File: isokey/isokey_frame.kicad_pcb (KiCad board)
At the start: 2 copper layers, 158.4 x 138.3 mm, 394 parts, among them J1 PJ-320A-4P, J2 PJ-320A-4P, Q2 BSS138, Q3 BSS138, SW1 Cherry, SW10 Cherry, SW11 Cherry, SW12 Cherry, SW13 Cherry, SW14 Cherry, SW15 Cherry, SW16 Cherry, SW17 Cherry, SW18 Cherry, SW19 Cherry, SW2 Cherry, SW20 Cherry, SW21 Cherry, SW22 Cherry, SW23 Cherry, SW24 Cherry, SW25 Cherry, SW26 Cherry, SW27 Cherry, SW28 Cherry, SW29 Cherry, SW3 Cherry, SW30 Cherry, SW31 Cherry, SW32 Cherry, SW33 Cherry, SW34 Cherry, SW35 Cherry, SW36 Cherry, SW37 Cherry, SW38 Cherry, SW39 Cherry, SW4 Cherry, SW40 Cherry, SW41 Cherry, SW42 Cherry, SW43 Cherry, SW44 Cherry, SW45 Cherry, SW46 Cherry, SW47 Cherry, SW48 Cherry, SW5 Cherry, SW6 Cherry, SW7 Cherry, SW8 Cherry, SW9 Cherry, U1 BlackPill_STLINK, U3 TLV73318PDBV, U6 JOYSTICKPTH, U7 JOYSTICKPTH, U9 TLV73318PDBV

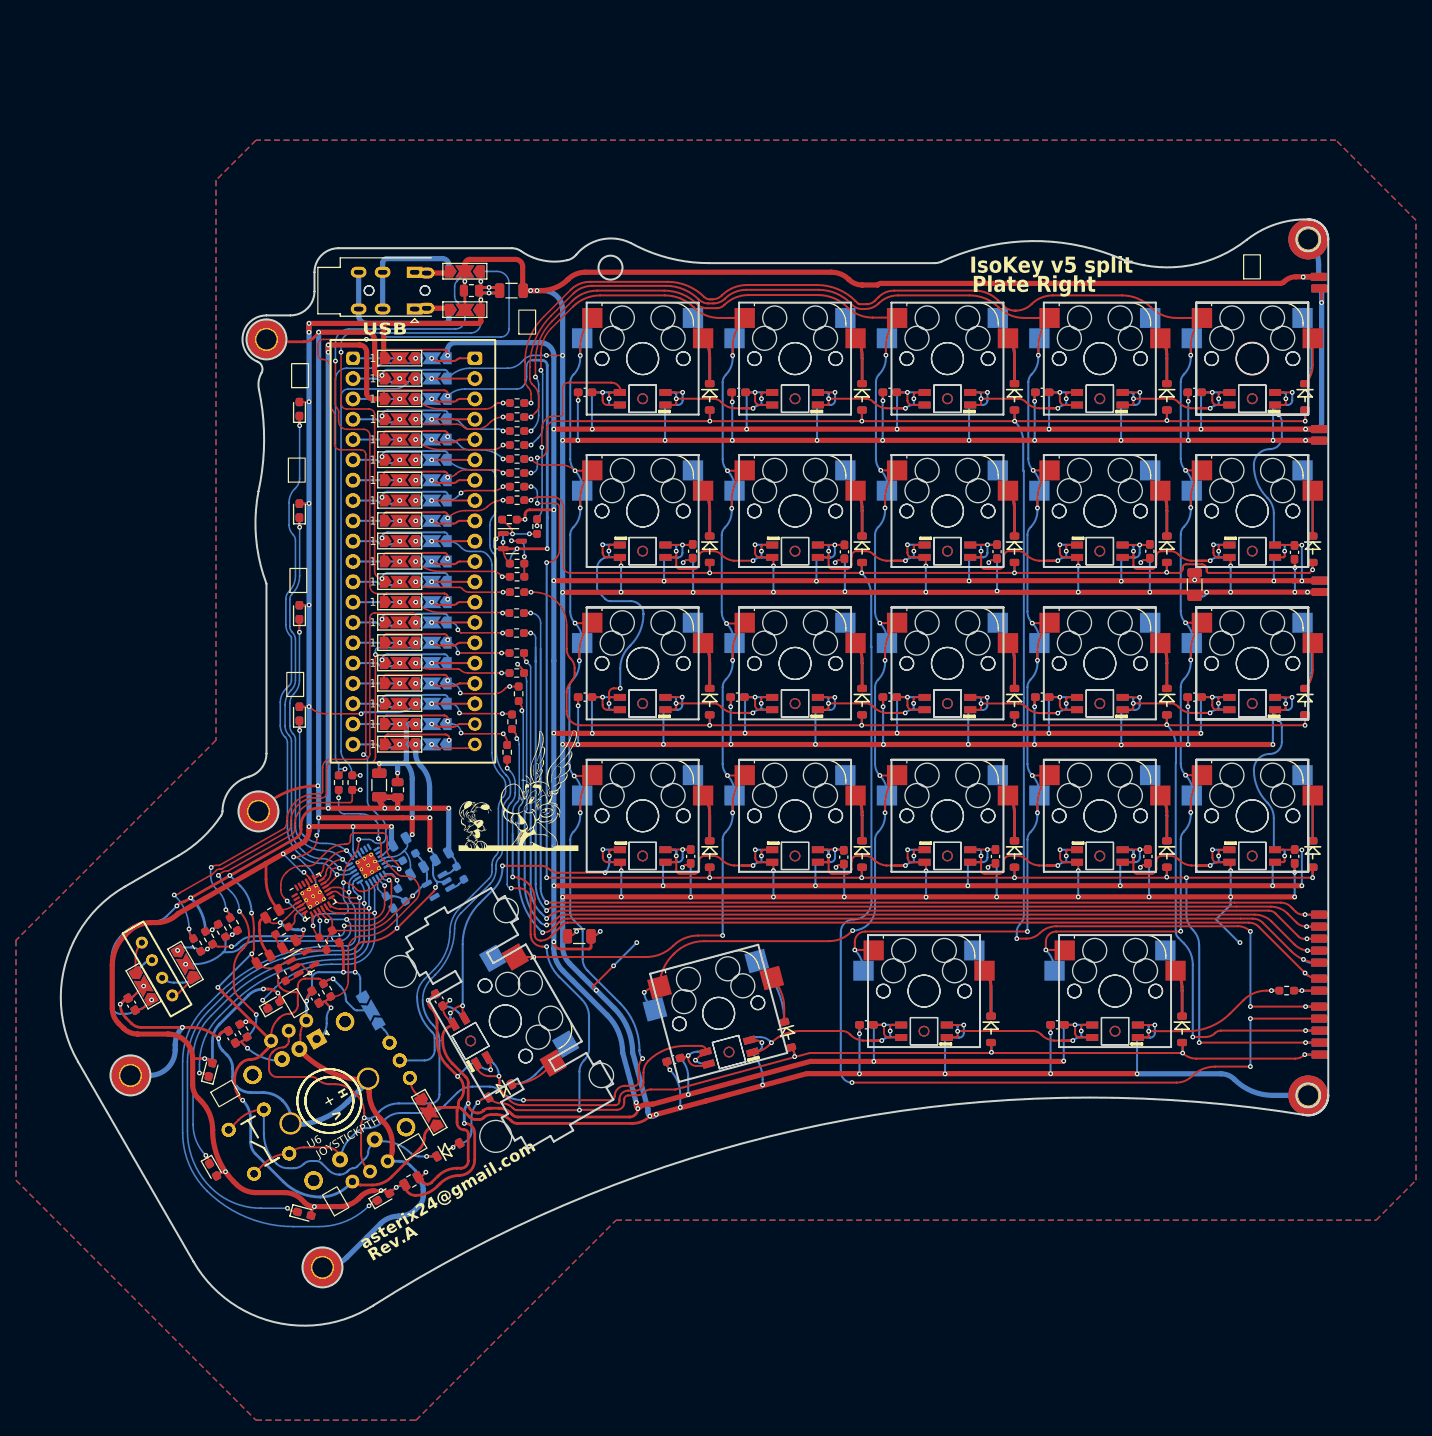
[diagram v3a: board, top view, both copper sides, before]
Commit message: add frame pcb
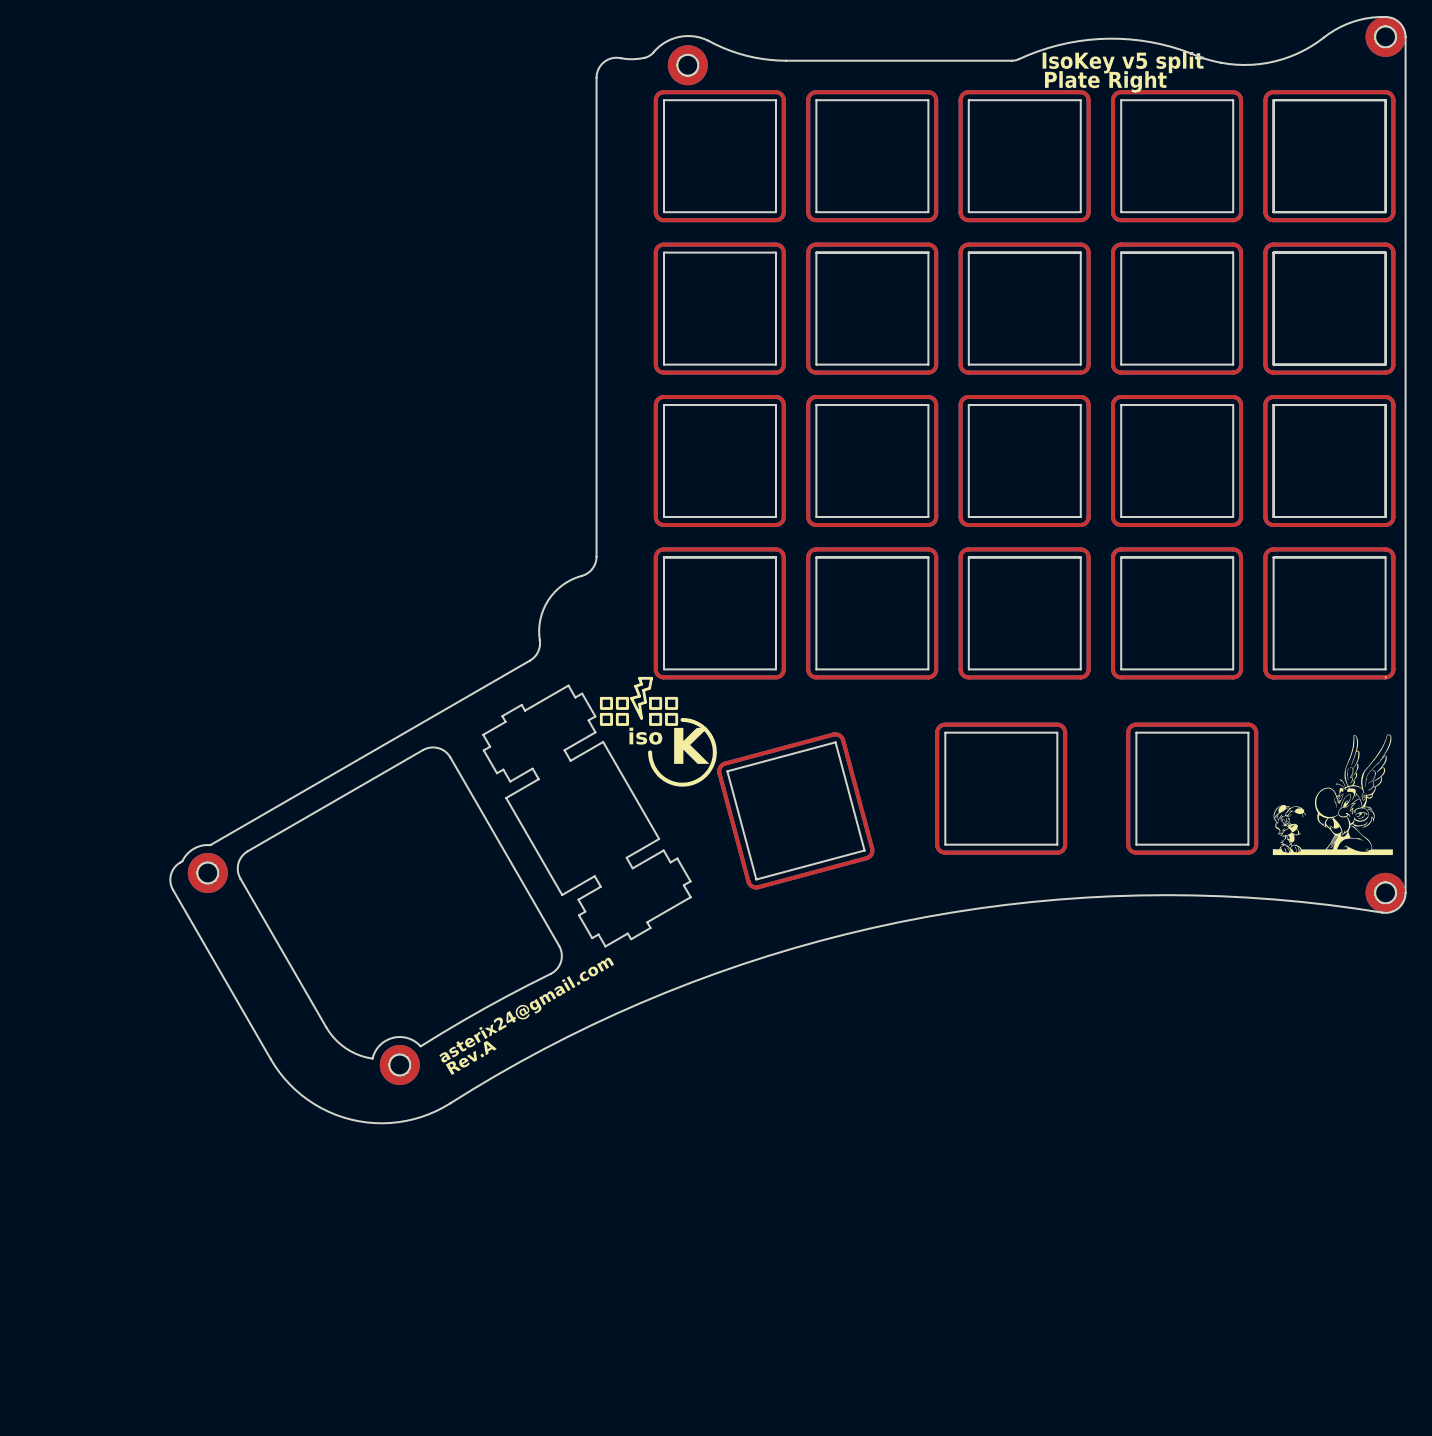
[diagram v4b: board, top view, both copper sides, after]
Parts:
- removed C1, C10, C11, C3, C38, C64, C71, C73, C74, C75, C87, C89: 1uF, Capacitor_SMD:C_0805_2012Metric
- removed C14, C15, C16, C17, C18, C19, C20, C21, C22, C23, C24, C25, C26, C27, C28, C29, C30, C31, C32, C33, C34, C35, C36, C37, C39, C40, C41, C42, C43, C44, C45, C46, C47, C48, C49, C50, C51, C52, C53, C54, C55, C56, C57, C58, C59, C60, C61, C62, C68, C69, C7, C70, C72, C8, C88, C9: 100nF, Capacitor_SMD:C_0603_1608Metric_Pad1.08x0.95mm_HandSolder
- removed C2, C4, C5, C6, C63, C65, C66, C67: 10uF, Capacitor_SMD:C_1206_3216Metric
- removed D1, D10, D11, D119, D12, D120, D121, D122, D123, D124, D125, D126, D127, D128, D129, D13, D130, D131, D132, D133, D134, D135, D136, D137, D138, D14, D15, D16, D17, D18, D19, D2, D20, D21, D22, D23, D24, D25, D26, D27, D28, D29, D3, D4, D5, D6, D7, D74, D8, D9: 1N4448W, Diode_SMD:D_SOD-123
- removed D110, D111, D112, D113, D114, D115, D116, D117, D118, D79, D80, D81, D82, D83, D84, D85, D86, D87: LED, LED_SMD:LED_0603_1608Metric_Pad1.05x0.95mm_HandSolder
- removed D30, D31, D32, D33, D34, D35, D36, D37, D38, D39, D40, D41, D42, D43, D44, D45, D46, D47, D48, D49, D50, D51, D52, D53, D54, D55, D56, D57, D58, D59, D60, D61, D62, D63, D64, D65, D66, D67, D68, D69, D70, D71, D72, D73, D75, D76, D77, D78: SK6812MINI-E, LED_SMD:LED_SK6812MINI_PLCC4_3.5x3.5mm_P1.75mm
- removed the G*** at (122.8, 161.3)
- removed the G*** at (124.1, 166.2)
- removed H1, H2, H3, H5, H6: MountingHole_Pad, MountingHole:MountingHole_2.5mm_Pad_TopBottom
- removed H4: StabilizerHoles, Button_Switch_Keyboard:Stabilizer_MX_2u
- removed J1, J2: PJ-320A-4P, Connector_Audio:Jack_3.5mm_PJ320E_Horizontal
- removed JP1, JP10, JP11, JP12, JP13, JP14, JP15, JP16, JP17, JP18, JP19, JP2, JP20, JP21, JP22, JP23, JP24, JP25, JP26, JP27, JP28, JP29, JP3, JP30, JP31, JP32, JP33, JP34, JP35, JP36, JP37, JP38, JP39, JP4, JP40, JP41, JP42, JP43, JP44, JP45, JP46, JP47, JP48, JP49, JP5, JP50, JP6, JP7, JP8, JP9: SolderJumper_3_Open_line, Jumper:SolderJumper-3_P2.0mm_Open_TrianglePad1.0x1.5mm_NumberLabels
- removed Q2, Q3: BSS138, Package_TO_SOT_SMD:SOT-23-3
- removed R1, R20: 4k7, Resistor_SMD:R_0603_1608Metric_Pad0.98x0.95mm_HandSolder
- removed R10, R11, R12, R13, R15, R17, R19, R2, R21, R23, R25, R27, R28, R29, R30, R31, R32, R33, R34, R35, R4, R42, R43, R44, R48, R49, R5, R50, R51, R52, R53, R54, R55, R56, R57, R58, R59, R6, R60, R61, R62, R63, R64, R7, R8, R9: 22R, Resistor_SMD:R_0603_1608Metric_Pad0.98x0.95mm_HandSolder
- removed R14, R16, R18, R22, R24, R26, R3, R36, R37, R38, R39, R40, R41, R46, R47, R65: 10k, Resistor_SMD:R_0603_1608Metric_Pad0.98x0.95mm_HandSolder
- removed RSW1: RotaryEncoder_Switch, Rotary_Encoder:RotaryEncoder_Alps_EC12E-Switch_Vertical_H20mm_CircularMountingHoles
- removed SW1, SW10, SW11, SW12, SW13, SW14, SW15, SW16, SW17, SW18, SW19, SW2, SW20, SW21, SW22, SW23, SW24, SW25, SW26, SW27, SW28, SW29, SW3, SW30, SW31, SW32, SW33, SW34, SW35, SW36, SW37, SW38, SW39, SW4, SW40, SW41, SW42, SW43, SW44, SW45, SW46, SW47, SW48, SW5, SW6, SW7, SW8, SW9: Cherry, Button_Switch_Keyboard:Kailh_socket_MX_LED
- removed TP1: CL6, TestPoint:Testpoint_Pad_1.0x2.0mm
- removed TP10, TP17, TP6: GND, TestPoint:Testpoint_Pad_1.0x2.0mm
- removed TP11: W1, TestPoint:Testpoint_Pad_1.0x2.0mm
- removed TP12: R0, TestPoint:Testpoint_Pad_1.0x2.0mm
- removed TP13: R1, TestPoint:Testpoint_Pad_1.0x2.0mm
- removed TP14: R2, TestPoint:Testpoint_Pad_1.0x2.0mm
- removed TP15: R3, TestPoint:Testpoint_Pad_1.0x2.0mm
- removed TP16: R4, TestPoint:Testpoint_Pad_1.0x2.0mm
- removed TP18, TP5, TP9: +5V, TestPoint:Testpoint_Pad_1.0x2.0mm
- removed TP2: CL7, TestPoint:Testpoint_Pad_1.0x2.0mm
- removed TP3: CL8, TestPoint:Testpoint_Pad_1.0x2.0mm
- removed TP4: CL9, TestPoint:Testpoint_Pad_1.0x2.0mm
- removed TP7: CL10, TestPoint:Testpoint_Pad_1.0x2.0mm
- removed TP8: ID, TestPoint:Testpoint_Pad_1.0x2.0mm
- removed U1: BlackPill_STLINK, Module:BlackPill
- removed U2: ~, Display:OLED_Display_128x32_SSD1306_i2c
- removed U3, U9: TLV73318PDBV, Package_TO_SOT_SMD:SOT-23-5
- removed U5, U8: ~, Package_DFN_QFN:WQFN-24-1EP_4x4mm_P0.5mm_EP2.45x2.45mm_ThermalVias
- removed U6, U7: JOYSTICKPTH, SparkFun-Electromechanical:JOYSTICK
- added G***: LOGO, footprints:logo_15x15, F.Cu at (224.6, 161.8)
- added G***: LOGO, footprints:logo_15x15, B.Cu at (224.7, 161.8)
- added H7: MountingHole_Pad, MountingHole:MountingHole_2.5mm_Pad_TopBottom, F.Cu at (108.0, 195.6)
- added H7: MountingHole_Pad, MountingHole:MountingHole_2.5mm_Pad_TopBottom, F.Cu at (231.2, 174.1)
- added H7: MountingHole_Pad, MountingHole:MountingHole_2.5mm_Pad_TopBottom, F.Cu at (231.2, 67.1)
- added H7: MountingHole_Pad, MountingHole:MountingHole_2.5mm_Pad_TopBottom, F.Cu at (84.0, 171.6)
- added REF**: isokey, footprints:isokey, F.Cu at (138.4, 160.9)
- added REF**: isokey, footprints:isokey, B.Cu at (147.4, 161.6)
- moved H7 80.5 mm to (144.0, 70.6)
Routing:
- net GND: track 1531.7 -> 0.00 mm, vias 151 -> 0
- net +5V: track 1219.1 -> 0.00 mm, vias 89 -> 0
- net +3.3V: track 341.4 -> 0.00 mm, vias 23 -> 0
- net /r1: track 253.8 -> 0.00 mm, vias 9 -> 0
- net /r0: track 231.9 -> 0.00 mm, vias 11 -> 0
- net /cl4: track 226.1 -> 0.00 mm, vias 10 -> 0
- net /cl3: track 211.7 -> 0.00 mm, vias 10 -> 0
- net /r3: track 201.5 -> 0.00 mm, vias 12 -> 0
- net /cl2: track 197.4 -> 0.00 mm, vias 11 -> 0
- net /cl0: track 186.3 -> 0.00 mm, vias 10 -> 0
- net /r2: track 184.1 -> 0.00 mm, vias 8 -> 0
- net /r4: track 177.9 -> 0.00 mm, vias 10 -> 0
- net /cl1: track 176.8 -> 0.00 mm, vias 11 -> 0
- net /cl5: track 137.5 -> 0.00 mm, vias 3 -> 0
- net /pb1: track 137.3 -> 0.00 mm, vias 2 -> 0
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- removed copper zone on B.Cu, net GND
- removed copper zone on F.Cu, net GND
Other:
- board size 158.4 x 138.3 mm -> 154.4 x 138.3 mm
- board text removed: "󰄼"
- board text removed: "󰚌"
- board text removed: "󰚫"
- board text removed: "󰛤"
- board text removed: "󰞷"
- board text removed: "󰠖"
- board text removed: "󰣘"
